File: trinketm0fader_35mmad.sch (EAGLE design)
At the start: 11 parts, among them IC1 74AHCT1G125DBV

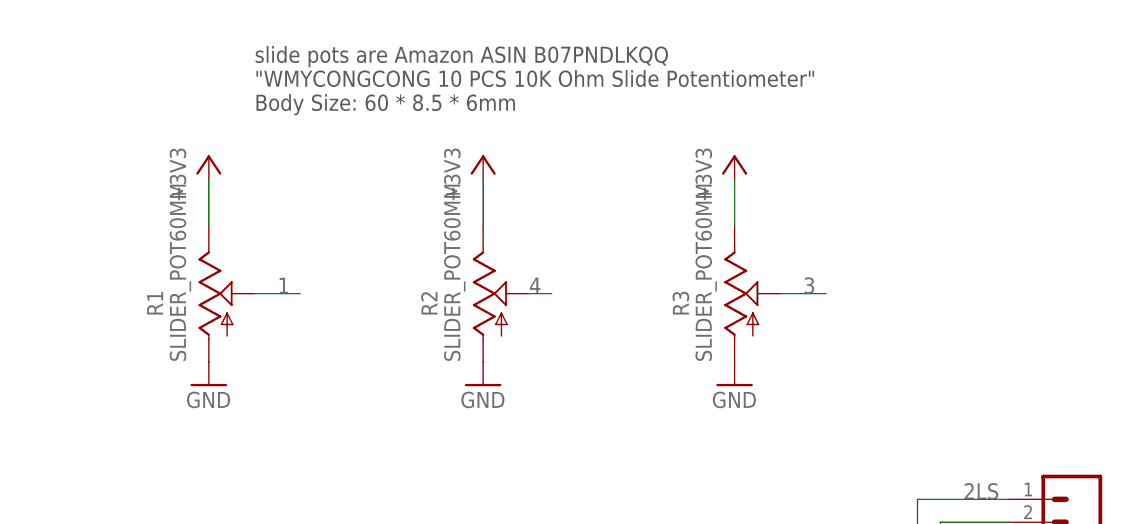
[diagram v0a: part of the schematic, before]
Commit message: added adafruit fader version
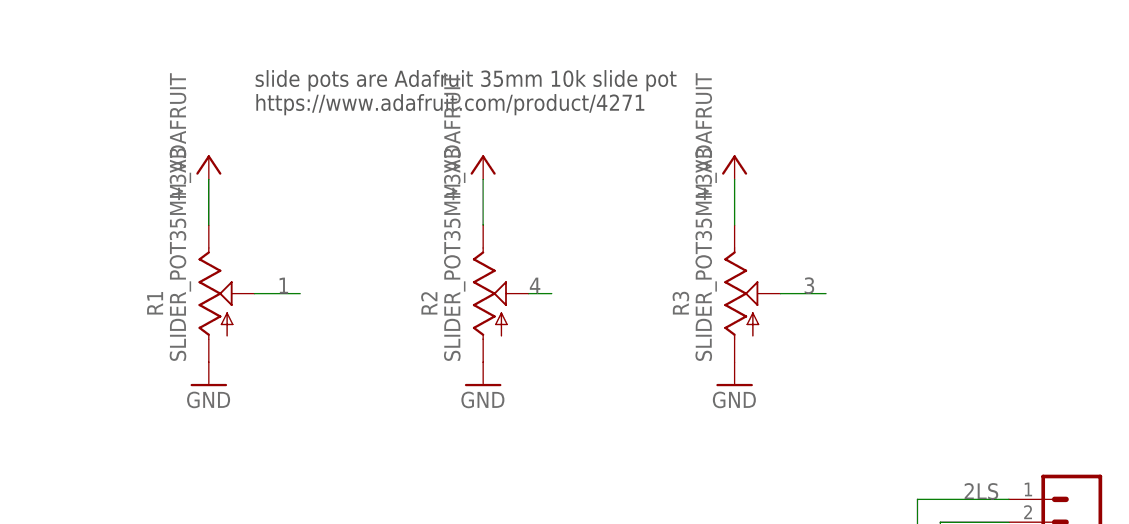
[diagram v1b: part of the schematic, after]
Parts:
- R1, R2, R3: value SLIDER_POT60MM -> SLIDER_POT35MM_ADAFRUIT; device todstuff:SLIDER_POT60MM -> todstuff:SLIDER_POT35MM_ADAFRUIT
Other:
- note added: "slide pots are Adafruit 35mm 10k slide pot https://www.adafruit.com/product/4271"
- note removed: "slide pots are Amazon ASIN B07PNDLKQQ "WMYCONGCONG 10 PCS 10K Ohm Slide Potentiometer" Body Size: 60 * 8.5 * 6mm"
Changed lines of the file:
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@@
 <grid distance="0.1" unitdist="inch" unit="inch" style="lines" multiple="1" display="no" altdistance="0.01" altunitdist="inch" altunit="inch"/>
 <layers>
-<layer number="1" name="Top" color="4" fill="1" visible="no" active="no"/>
-<layer number="2" name="Route2" color="16" fill="1" visible="no" active="no"/>
-<layer number="3" name="Route3" color="17" fill="1" visible="no" active="no"/>
-<layer number="4" name="Route4" color="18" fill="1" visible="no" active="no"/>
-<layer number="5" name="Route5" color="19" fill="1" visible="no" active="no"/>
-<layer number="6" name="Route6" color="25" fill="1" visible="no" active="no"/>
-<layer number="7" name="Route7" color="26" fill="1" visible="no" active="no"/>
-<layer number="8" name="Route8" color="27" fill="1" visible="no" active="no"/>
-<layer number="9" name="Route9" color="28" fill="1" visible="no" active="no"/>
-<layer number="10" name="Route10" color="29" fill="1" visible="no" active="no"/>
-<layer number="11" name="Route11" color="30" fill="1" visible="no" active="no"/>
-<layer number="12" name="Route12" color="20" fill="1" visible="no" active="no"/>
-<layer number="13" name="Route13" color="21" fill="1" visible="no" active="no"/>
-<layer number="14" name="Route14" color="22" fill="1" visible="no" active="no"/>
-<layer number="15" name="Route15" color="23" fill="1" visible="no" active="no"/>
-<layer number="16" name="Bottom" color="1" fill="1" visible="no" active="no"/>
-<layer number="17" name="Pads" color="2" fill="1" visible="no" active="no"/>
-<layer number="18" name="Vias" color="2" fill="1" visible="no" active="no"/>
-<layer number="19" name="Unrouted" color="6" fill="1" visible="no" active="no"/>
-<layer number="20" name="Dimension" color="7" fill="1" visible="no" active="no"/>
-<layer number="21" name="tPlace" color="7" fill="1" visible="no" active="no"/>
-<layer number="22" name="bPlace" color="7" fill="1" visible="no" active="no"/>
-<layer number="23" name="tOrigins" color="15" fill="1" visible="no" active="no"/>
-<layer number="24" name="bOrigins" color="15" fill="1" visible="no" active="no"/>
-<layer number="25" name="tNames" color="7" fill="1" visible="no" active="no"/>
-<layer number="26" name="bNames" color="7" fill="1" visible="no" active="no"/>
-<layer number="27" name="tValues" color="7" fill="1" visible="no" active="no"/>
-<layer number="28" name="bValues" color="7" fill="1" visible="no" active="no"/>
+<layer number="1" name="Top" color="4" fill="1" visible="yes" active="no"/>
+<layer number="2" name="Route2" color="16" fill="1" visible="yes" active="no"/>
+<layer number="3" name="Route3" color="17" fill="1" visible="yes" active="no"/>
+<layer number="4" name="Route4" color="18" fill="1" visible="yes" active="no"/>
+<layer number="5" name="Route5" color="19" fill="1" visible="yes" active="no"/>
+<layer number="6" name="Route6" color="25" fill="1" visible="yes" active="no"/>
+<layer number="7" name="Route7" color="26" fill="1" visible="yes" active="no"/>
+<layer number="8" name="Route8" color="27" fill="1" visible="yes" active="no"/>
+<layer number="9" name="Route9" color="28" fill="1" visible="yes" active="no"/>
+<layer number="10" name="Route10" color="29" fill="1" visible="yes" active="no"/>
+<layer number="11" name="Route11" color="30" fill="1" visible="yes" active="no"/>
+<layer number="12" name="Route12" color="20" fill="1" visible="yes" active="no"/>
+<layer number="13" name="Route13" color="21" fill="1" visible="yes" active="no"/>
+<layer number="14" name="Route14" color="22" fill="1" visible="yes" active="no"/>
+<layer number="15" name="Route15" color="23" fill="1" visible="yes" active="no"/>
+<layer number="16" name="Bottom" color="1" fill="1" visible="yes" active="no"/>
+<layer number="17" name="Pads" color="2" fill="1" visible="yes" active="no"/>
+<layer number="18" name="Vias" color="2" fill="1" visible="yes" active="no"/>
+<layer number="19" name="Unrouted" color="6" fill="1" visible="yes" active="no"/>
+<layer number="20" name="Dimension" color="7" fill="1" visible="yes" active="no"/>
+<layer number="21" name="tPlace" color="7" fill="1" visible="yes" active="no"/>
+<layer number="22" name="bPlace" color="7" fill="1" visible="yes" active="no"/>
+<layer number="23" name="tOrigins" color="15" fill="1" visible="yes" active="no"/>
+<layer number="24" name="bOrigins" color="15" fill="1" visible="yes" active="no"/>
+<layer number="25" name="tNames" color="7" fill="1" visible="yes" active="no"/>
+<layer number="26" name="bNames" color="7" fill="1" visible="yes" active="no"/>
+<layer number="27" name="tValues" color="7" fill="1" visible="yes" active="no"/>
+<layer number="28" name="bValues" color="7" fill="1" visible="yes" active="no"/>
 <layer number="29" name="tStop" color="7" fill="3" visible="no" active="no"/>
 <layer number="30" name="bStop" color="7" fill="6" visible="no" active="no"/>
@@
 <layer number="35" name="tGlue" color="7" fill="4" visible="no" active="no"/>
 <layer number="36" name="bGlue" color="7" fill="5" visible="no" active="no"/>
-<layer number="37" name="tTest" color="7" fill="1" visible="no" active="no"/>
-<layer number="38" name="bTest" color="7" fill="1" visible="no" active="no"/>
+<layer number="37" name="tTest" color="7" fill="1" visible="yes" active="no"/>
+<layer number="38" name="bTest" color="7" fill="1" visible="yes" active="no"/>
 <layer number="39" name="tKeepout" color="4" fill="11" visible="no" active="no"/>
 <layer number="40" name="bKeepout" color="1" fill="11" visible="no" active="no"/>
@@
 <layer number="44" name="Drills" color="7" fill="1" visible="no" active="no"/>
 <layer number="45" name="Holes" color="7" fill="1" visible="no" active="no"/>
-<layer number="46" name="Milling" color="3" fill="1" visible="no" active="no"/>
-<layer number="47" name="Measures" color="7" fill="1" visible="no" active="no"/>
-<layer number="48" name="Document" color="7" fill="1" visible="no" active="no"/>
-<layer number="49" name="Reference" color="7" fill="1" visible="no" active="no"/>
-<layer number="50" name="dxf" color="7" fill="1" visible="no" active="no"/>
-<layer number="51" name="tDocu" color="7" fill="1" visible="no" active="no"/>
-<layer number="52" name="bDocu" color="7" fill="1" visible="no" active="no"/>
-<layer number="53" name="tGND_GNDA" color="7" fill="9" visible="no" active="no"/>
-<layer number="54" name="bGND_GNDA" color="1" fill="9" visible="no" active="no"/>
-<layer number="56" name="wert" color="7" fill="1" visible="no" active="no"/>
-<layer number="57" name="tCAD" color="7" fill="1" visible="no" active="no"/>
-<layer number="59" name="tCarbon" color="7" fill="1" visible="no" active="no"/>
-<layer number="60" name="bCarbon" color="7" fill="1" visible="no" active="no"/>
+<layer number="46" name="Milling" color="3" fill="1" visible="yes" active="no"/>
+<layer number="47" name="Measures" color="7" fill="1" visible="yes" active="no"/>
+<layer number="48" name="Document" color="7" fill="1" visible="yes" active="no"/>
+<layer number="49" name="Reference" color="7" fill="1" visible="yes" active="no"/>
+<layer number="50" name="dxf" color="7" fill="1" visible="yes" active="no"/>
+<layer number="51" name="tDocu" color="7" fill="1" visible="yes" active="no"/>
+<layer number="52" name="bDocu" color="7" fill="1" visible="yes" active="no"/>
+<layer number="53" name="tGND_GNDA" color="7" fill="9" visible="yes" active="no"/>
+<layer number="54" name="bGND_GNDA" color="1" fill="9" visible="yes" active="no"/>
+<layer number="56" name="wert" color="7" fill="1" visible="yes" active="no"/>
+<layer number="57" name="tCAD" color="7" fill="1" visible="yes" active="no"/>
+<layer number="59" name="tCarbon" color="7" fill="1" visible="yes" active="no"/>
+<layer number="60" name="bCarbon" color="7" fill="1" visible="yes" active="no"/>
 <layer number="88" name="SimResults" color="9" fill="1" visible="yes" active="yes"/>
 <layer number="89" name="SimProbes" color="9" fill="1" visible="yes" active="yes"/>
@@
 <part name="P+3" library="supply1" library_urn="urn:adsk.eagle:library:371" deviceset="+5V" device=""/>
 <part name="GND4" library="supply1" library_urn="urn:adsk.eagle:library:371" deviceset="GND" device=""/>
-<part name="R1" library="todstuff" library_urn="urn:adsk.eagle:library:1731349" deviceset="SLIDER_POT" device="60MM" value="SLIDER_POT60MM"/>
-<part name="R2" library="todstuff" library_urn="urn:adsk.eagle:library:1731349" deviceset="SLIDER_POT" device="60MM" value="SLIDER_POT60MM"/>
-<part name="R3" library="todstuff" library_urn="urn:adsk.eagle:library:1731349" deviceset="SLIDER_POT" device="60MM" value="SLIDER_POT60MM"/>
+<part name="R1" library="todstuff" library_urn="urn:adsk.eagle:library:1731349" deviceset="SLIDER_POT" device="35MM_ADAFRUIT" value="SLIDER_POT35MM_ADAFRUIT"/>
+<part name="R2" library="todstuff" library_urn="urn:adsk.eagle:library:1731349" deviceset="SLIDER_POT" device="35MM_ADAFRUIT" value="SLIDER_POT35MM_ADAFRUIT"/>
+<part name="R3" library="todstuff" library_urn="urn:adsk.eagle:library:1731349" deviceset="SLIDER_POT" device="35MM_ADAFRUIT" value="SLIDER_POT35MM_ADAFRUIT"/>
 <part name="R4" library="rcl" library_urn="urn:adsk.eagle:library:334" deviceset="R-EU_" device="R0603" package3d_urn="urn:adsk.eagle:package:23555/3" value="500"/>
 <part name="J3" library="SparkFun-Connectors" library_urn="urn:adsk.eagle:library:513" deviceset="CONN_03" device="" package3d_urn="urn:adsk.eagle:package:38063/1"/>
@@
 <wire x1="5.08" y1="7.62" x2="5.08" y2="38.1" width="0.1524" layer="97"/>
 <text x="48.26" y="8.89" size="1.778" layer="97">TrinketM0</text>
-<text x="55.88" y="88.9" size="1.778" layer="97">slide pots are Amazon ASIN B07PNDLKQQ
-"WMYCONGCONG 10 PCS 10K Ohm Slide Potentiometer"
-Body Size: 60 * 8.5 * 6mm
+<text x="55.88" y="88.9" size="1.778" layer="97">slide pots are Adafruit 35mm 10k slide pot
+https://www.adafruit.com/product/4271
 </text>
 <text x="101.6" y="5.08" size="1.778" layer="97">or SN74LV1T125DCKR</text>
